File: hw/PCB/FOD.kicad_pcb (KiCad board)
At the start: 2 copper layers, 24 parts, among them J1 USB_B_Micro, J2 Programmer, J3 SMA, U0 AP7215-33YG-13, U1 SAMD21G, U4 RFM69HCW, Y1 32.768kHz

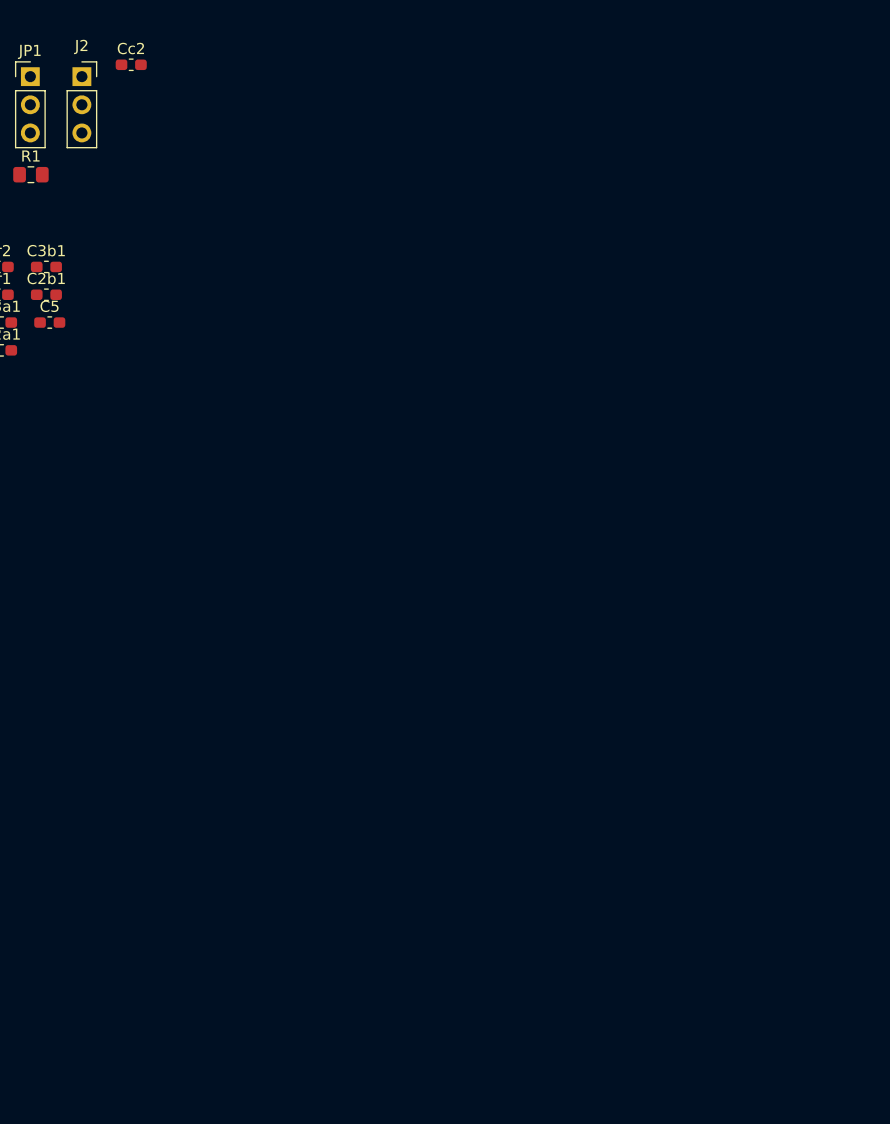
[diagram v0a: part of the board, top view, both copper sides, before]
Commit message: Updated PCB's schematic.
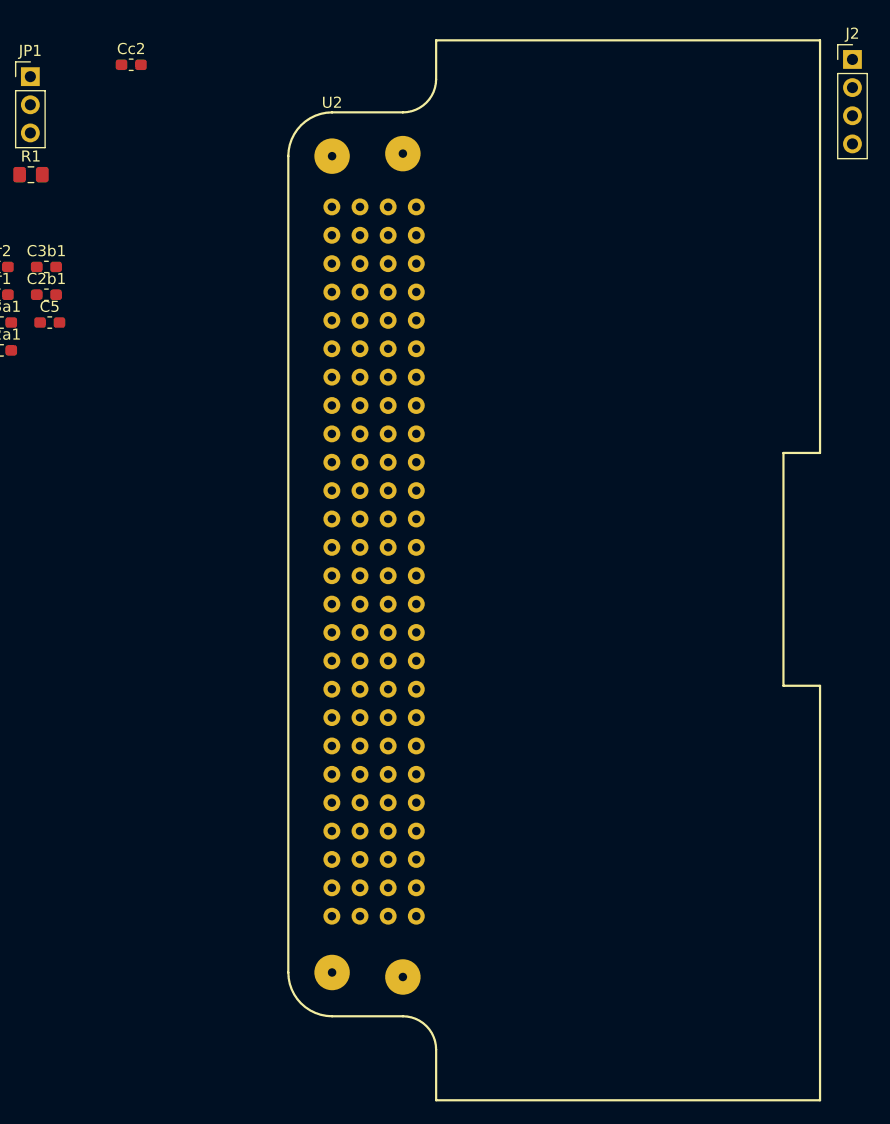
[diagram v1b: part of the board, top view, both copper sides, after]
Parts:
- added U2: Payload, Payload:FOD, F.Cu at (216.8, 147.8)
- J2: footprint Connector_PinSocket_2.54mm:PinSocket_1x03_P2.54mm_Vertical -> Connector_PinHeader_2.54mm:PinHeader_1x04_P2.54mm_Vertical
- moved J2 69.5 mm to (263.7, 65.4)

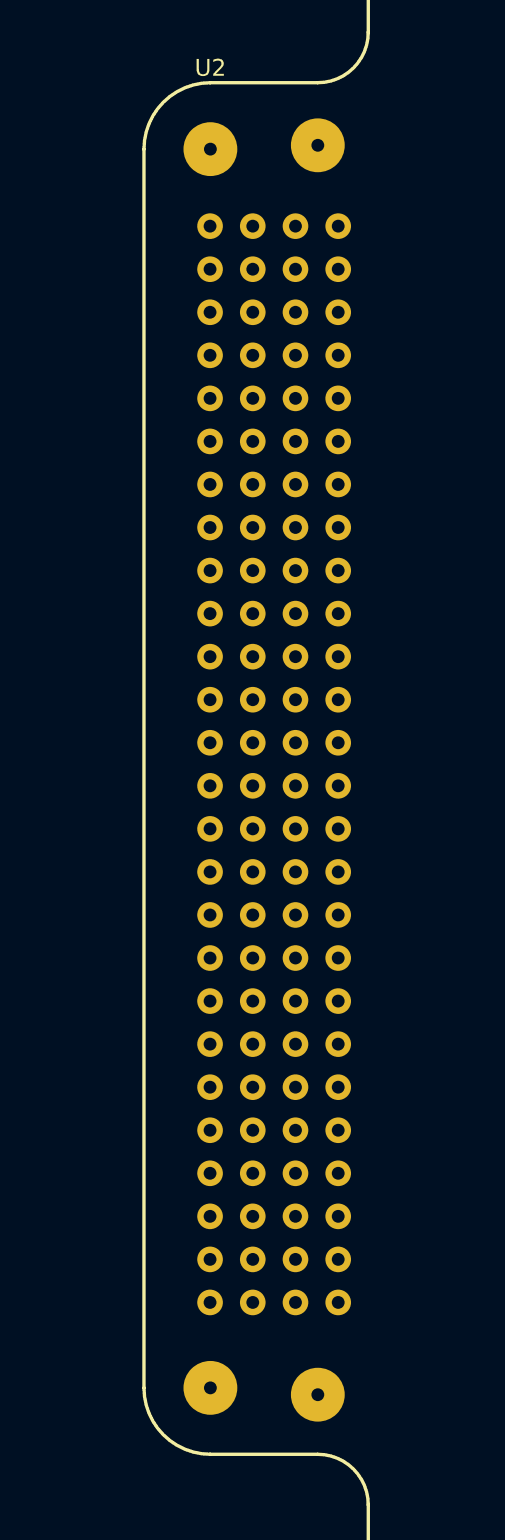
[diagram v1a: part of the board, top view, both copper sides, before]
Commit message: Updated the connections and the footprints asignation.
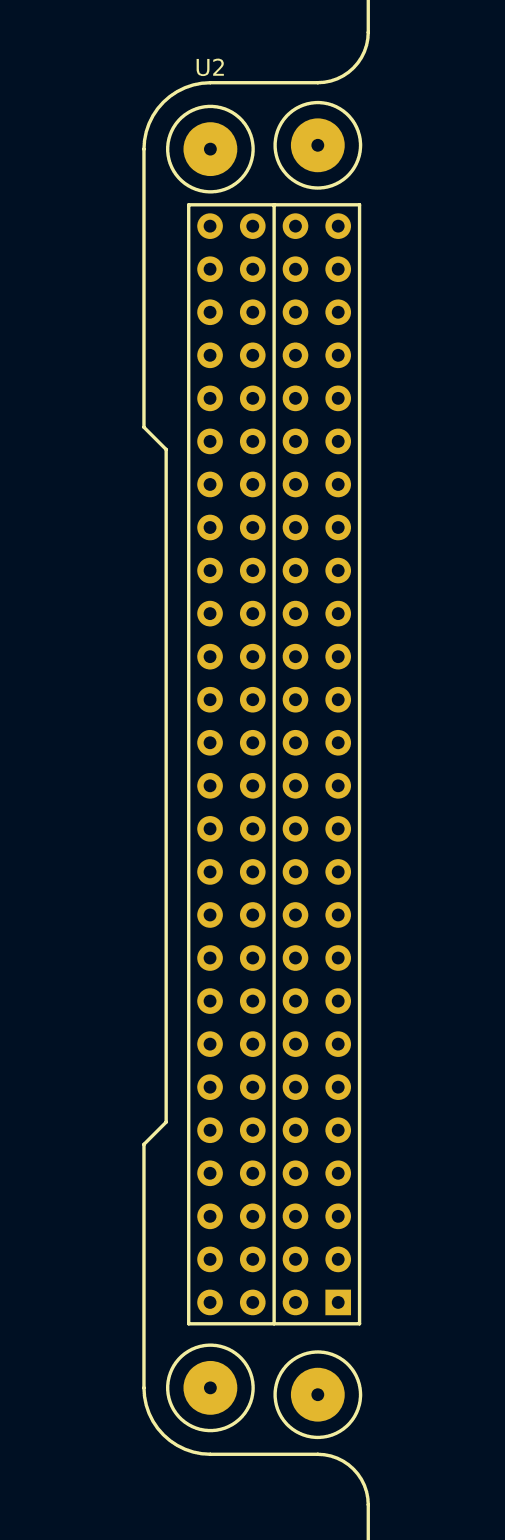
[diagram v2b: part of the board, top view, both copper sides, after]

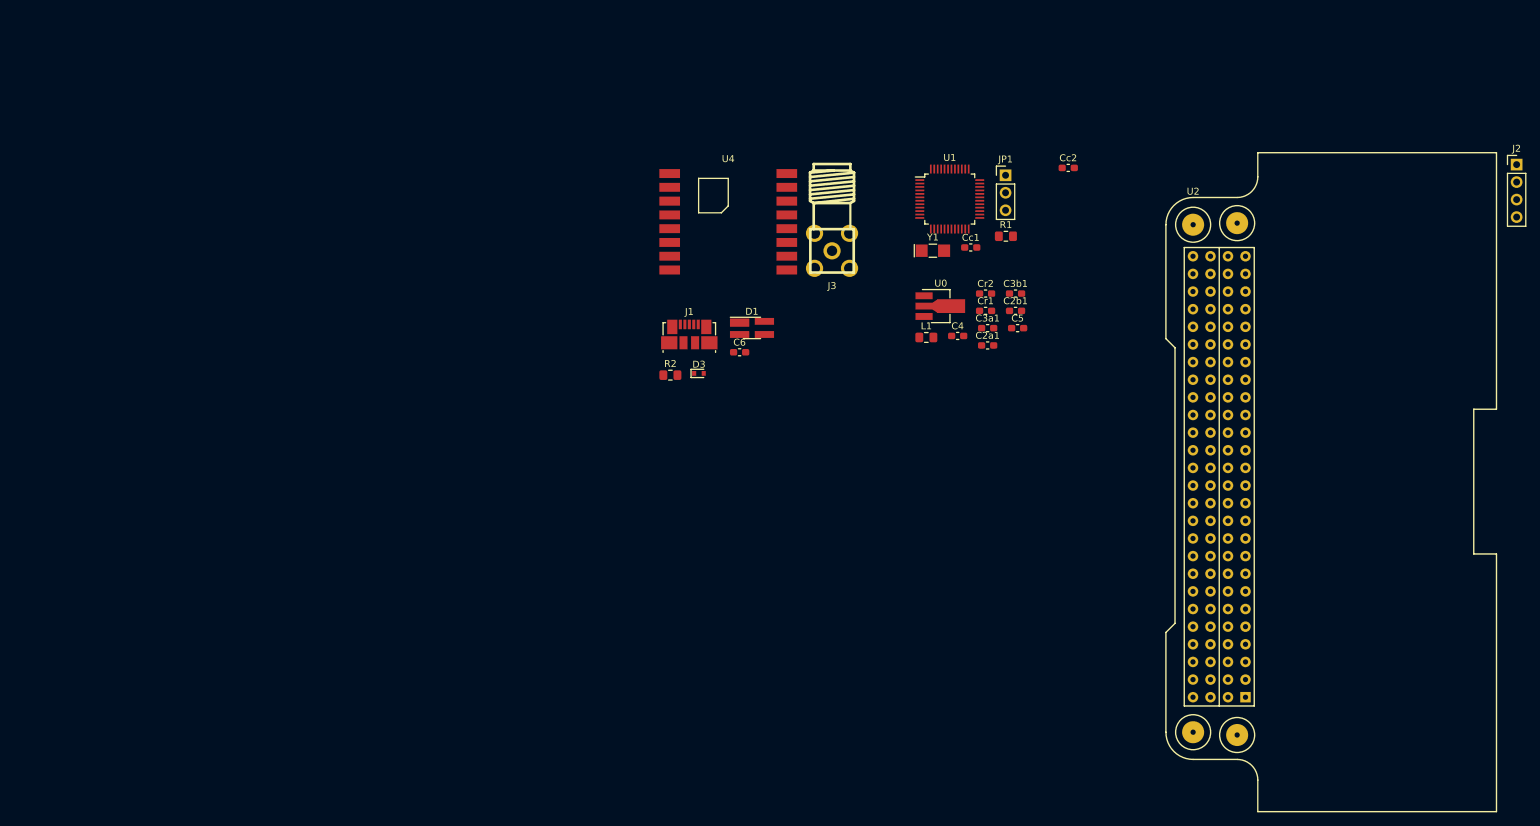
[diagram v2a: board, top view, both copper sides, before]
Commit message: Added the deployment system to the board's footprint.
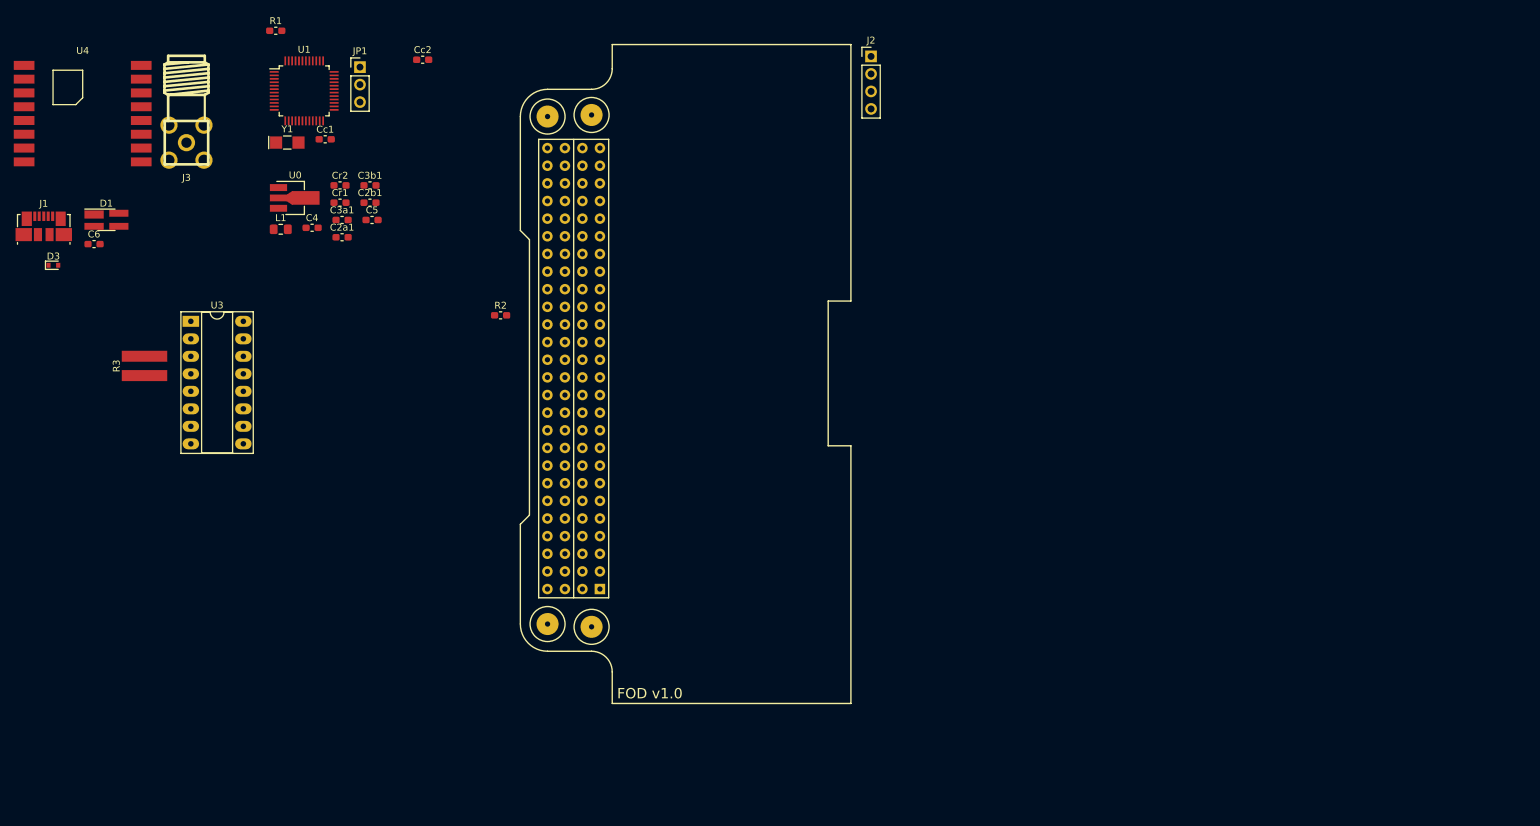
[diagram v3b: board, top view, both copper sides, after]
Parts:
- added R3: 7.15, Resistor_FOD:RCL12257R15FKEG, F.Cu at (64.5, 94.6)
- added U3: SN754410, Package_DIP:DIP-16_W7.62mm_Socket_LongPads, F.Cu at (71.3, 88.1)
- R1, R2: footprint Resistor_SMD:R_0805_2012Metric_Pad1.15x1.40mm_HandSolder -> Resistor_SMD:R_0603_1608Metric_Pad1.05x0.95mm_HandSolder
- moved R1 110.1 mm to (83.6, 46.0)
- moved C6 95.0 mm to (57.2, 76.9)
- moved C2a1 95.0 mm to (93.2, 75.9)
- moved C3a1 95.0 mm to (93.2, 73.4)
- moved C5 95.0 mm to (97.6, 73.4)
- moved Cc2 95.0 mm to (104.9, 50.2)
- moved Cr1 95.0 mm to (92.9, 70.9)
- moved Cr2 95.0 mm to (92.9, 68.4)
- moved D3 95.0 mm to (51.3, 80.0)
- moved J3 95.0 mm to (70.6, 62.2)
- moved JP1 95.0 mm to (95.8, 51.2)
- moved L1 95.0 mm to (84.3, 74.8)
- moved U0 95.0 mm to (86.0, 70.2)
- moved U1 95.0 mm to (87.7, 54.7)
- moved U2 95.0 mm to (123.1, 132.1)
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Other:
- board text added: "FOD v1.0"
